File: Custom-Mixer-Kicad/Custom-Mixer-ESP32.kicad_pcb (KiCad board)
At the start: 2 copper layers, 176.3 x 110.6 mm, 21 parts, among them J1 OLED1, J2 OLED2, J3 OLED3, J4 OLED4, J5 OLED5, SW1 RotaryEncoder_Switch, SW2 RotaryEncoder_Switch, U1 ESP32-DevKitC, U2 2717

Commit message: Cad Revision
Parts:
- added G***: LOGO, Custom-Mixer-Kicad:Hackclublogo(fmask), F.Cu at (214.4, 122.5)
- added REF**: MountingHole_3.2mm_M3, MountingHole:MountingHole_3.2mm_M3, F.Cu at (75.3, 44.2)
- added REF**: MountingHole_3.2mm_M3, MountingHole:MountingHole_3.2mm_M3, F.Cu at (231.6, 134.8)
- added kibuzzard-69777CED: G***, kibuzzard-69777CED, B.Cu at (149.6, 117.7)
- added kibuzzard-69777D46: G***, kibuzzard-69777D46, B.Cu at (149.2, 111.8)
- G***: footprint Custom-Mixer-ESP32:Hackclublogo -> Custom-Mixer-Kicad:Hackclublogo
- moved G*** 2.72 mm to (214.4, 122.5)
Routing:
- net Net-(U1-GPIO23): track 122.8 -> 119.4 mm
- added copper zone on B.Cu, net GND
- added copper zone on F.Cu, net GND

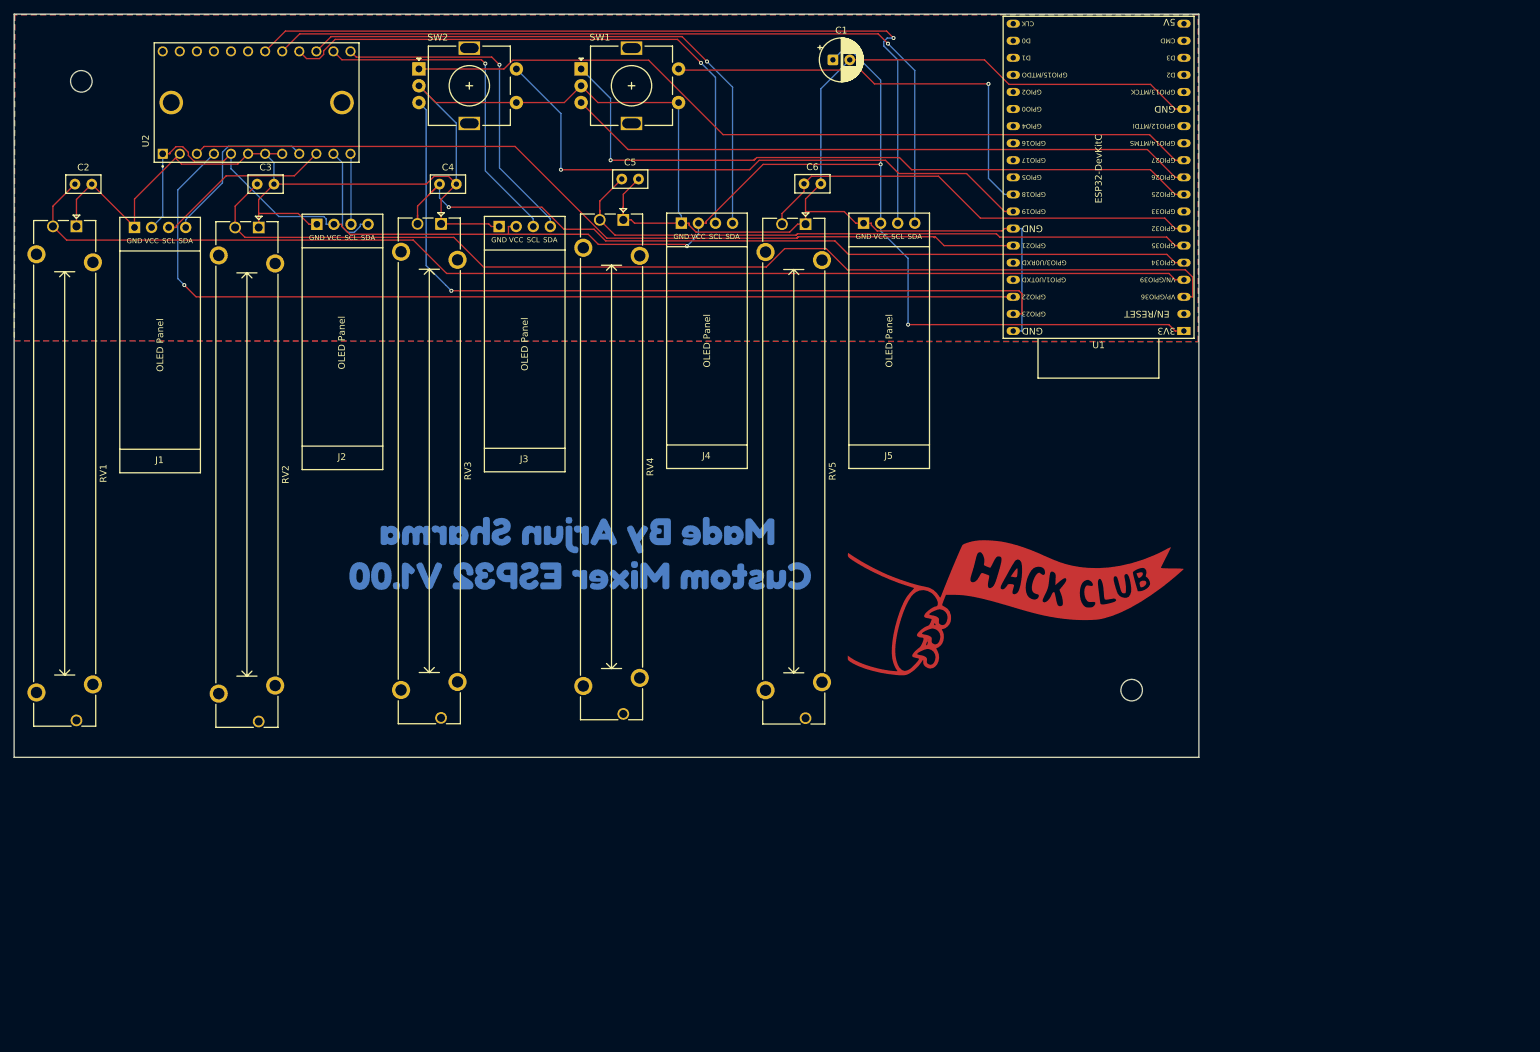
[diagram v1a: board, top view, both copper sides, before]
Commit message: Connect potentiometer pads to +3V3 and clean up nets
Updated RV2, RV3, and RV4 potentiometer pad 3 connections from unconnected nets to +3V3. Cleaned up and renumbered net assignments throughout the schematic, removed unused/unconnected net definitions, and adjusted component positions and silkscreen text for improved clarity.
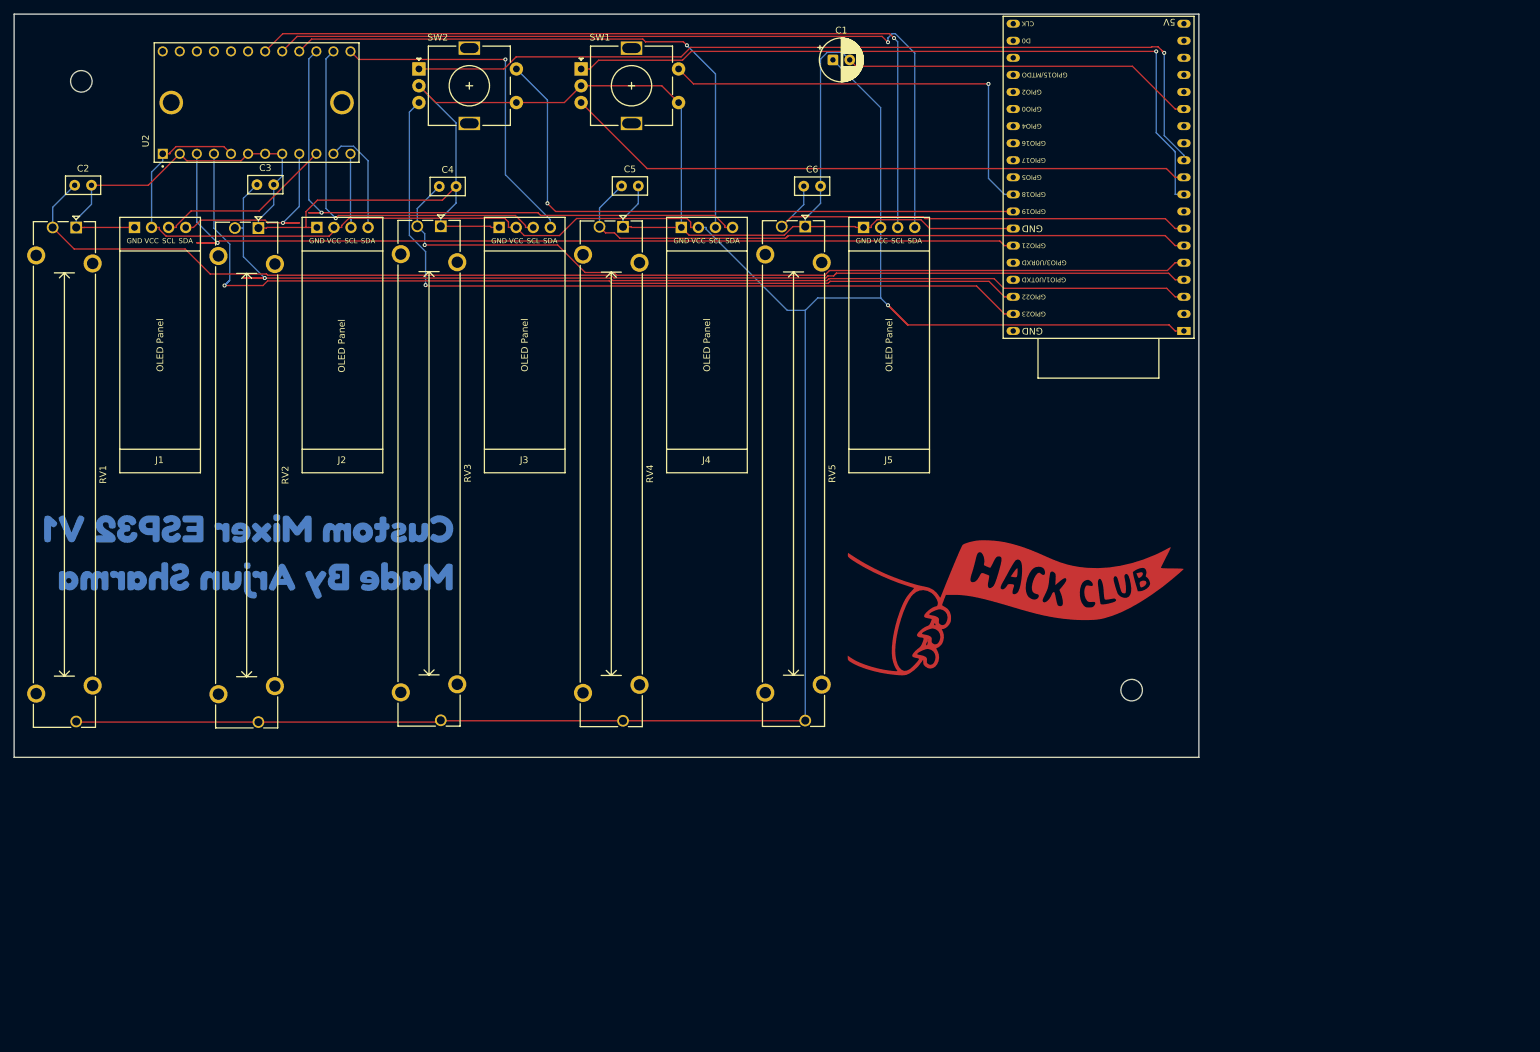
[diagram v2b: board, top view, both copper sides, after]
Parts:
- removed kibuzzard-69777CED: G***, kibuzzard-69777CED
- removed kibuzzard-69777D46: G***, kibuzzard-69777D46
- added kibuzzard-697B9E82: G***, kibuzzard-697B9E82, B.Cu at (100.2, 114.9)
- moved RV4 1.03 mm to (155.9, 65.9)
- moved C5 1.03 mm to (155.7, 59.8)
- moved J4 0.63 mm to (162.4, 102.5)
- moved J5 0.63 mm to (189.5, 102.5)
- moved J2 0.47 mm to (108.2, 102.5)
- moved C6 0.36 mm to (182.8, 59.8)
- moved RV5 0.36 mm to (183.1, 65.8)
- moved C4 0.35 mm to (128.6, 59.9)
- moved RV3 0.35 mm to (128.8, 65.8)
- moved RV1 0.17 mm to (74.6, 66.0)
- moved C2 0.17 mm to (74.4, 59.7)
- moved J3 0.14 mm to (135.3, 102.5)
- moved C3 0.09 mm to (101.5, 59.6)
- moved RV2 0.09 mm to (101.7, 66.1)
- renumbered G*** to Hackclublogo, REF** to REF1, REF** to REF2
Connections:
- RV1 pad 3: unconnected-(RV1-Pad3) -> +3V3
- RV2 pad 3: unconnected-(RV2-Pad3) -> +3V3
- RV3 pad 3: unconnected-(RV3-Pad3) -> +3V3
- RV4 pad 3: unconnected-(RV4-Pad3) -> +3V3
- RV5 pad 3: unconnected-(RV5-Pad3) -> +3V3
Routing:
- net +3V3: track 225.5 -> 415.2 mm, vias 3 -> 1
- net GND: track 357.3 -> 339.2 mm
- net Net-(U1-GPIO21): track 128.7 -> 145.6 mm, vias 0 -> 1
- net Net-(U1-ADC2_CH7/GPIO27): track 120.5 -> 131.9 mm, vias 0 -> 1
- net Net-(J1-Pin_4): track 25.7 -> 36.1 mm, vias 0 -> 1
- net Net-(J4-Pin_4): track 86.2 -> 95.1 mm
- net Net-(U1-SENSOR_VP/GPIO36/ADC1_CH0): track 159.8 -> 168.3 mm, vias 0 -> 1
- net Net-(U1-DAC_1/ADC2_CH8/GPIO25): track 103.4 -> 110.6 mm
- net Net-(J3-Pin_3): track 50.5 -> 56.3 mm
- net Net-(U1-GPIO22): track 146.2 -> 141.8 mm
- net Net-(J5-Pin_4): track 120.2 -> 123.4 mm
- net Net-(U1-GPIO19): track 88.8 -> 91.7 mm
- net Net-(U1-VDET_1/GPIO34/ADC1_CH6): track 127.7 -> 126.1 mm
- net Net-(J5-Pin_3): track 124.7 -> 123.3 mm
- net Net-(U1-VDET_2/GPIO35/ADC1_CH7): track 97.5 -> 96.1 mm
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- removed copper zone on B.Cu, net GND
- removed copper zone on F.Cu, net GND

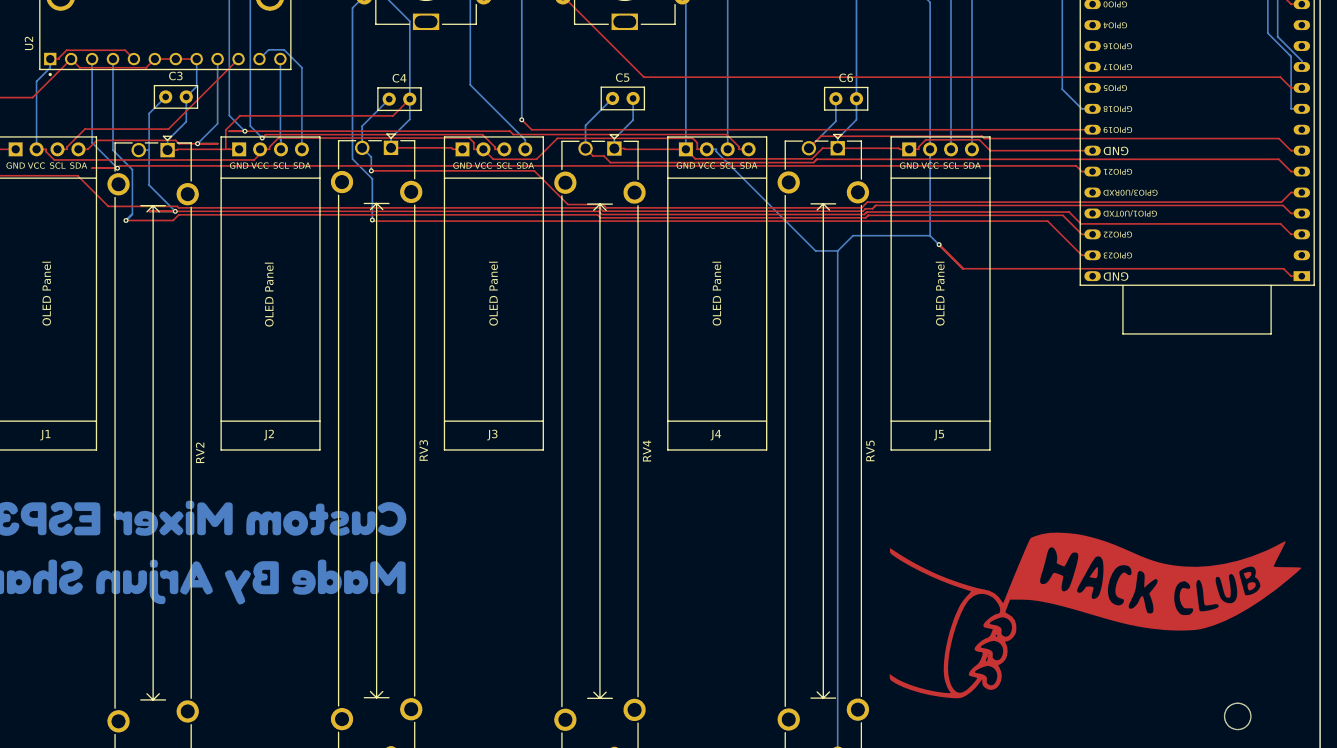
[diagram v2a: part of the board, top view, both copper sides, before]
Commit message: Add +3V3 power symbols and update PCB routing
Added multiple +3V3 power symbols to the schematic for improved clarity and power distribution. Updated PCB routing for nets 1 and 7, including new segments, vias, and changes to net connections for better signal integrity and layout. Adjusted positions of Hackclublogo footprints.
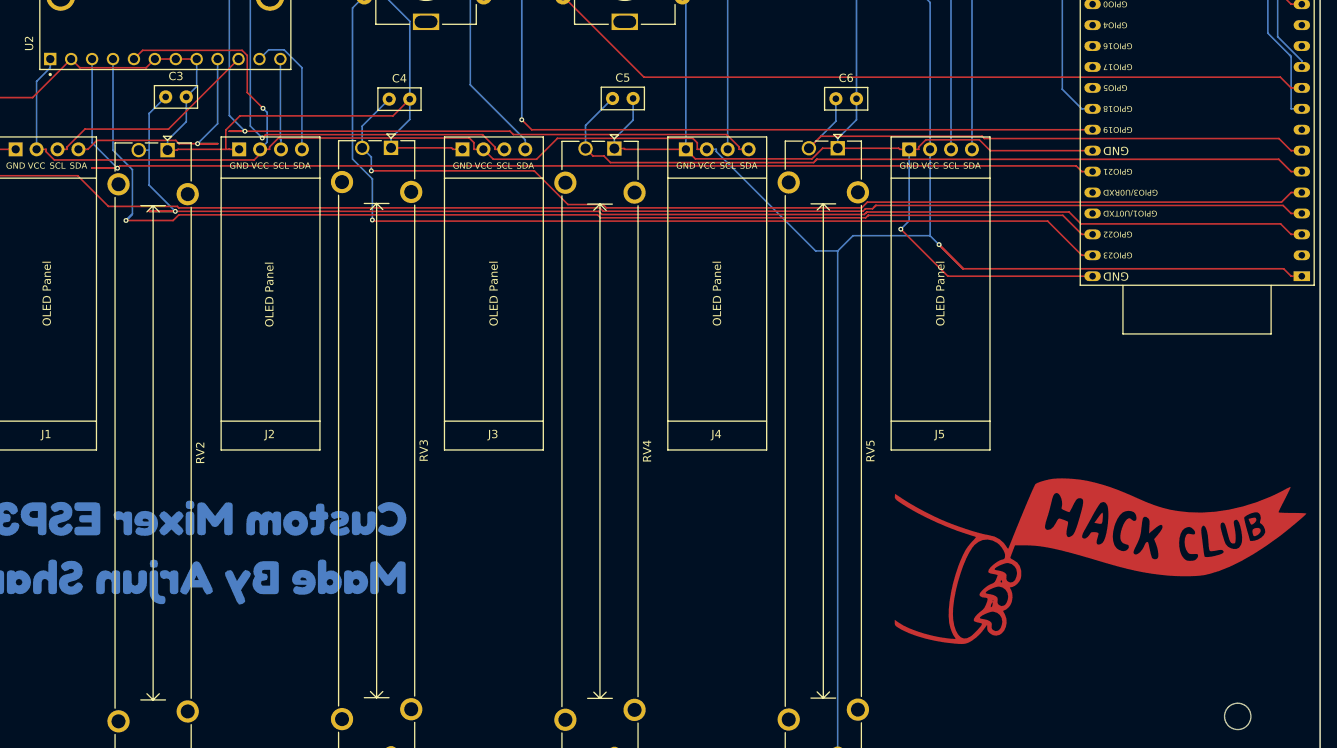
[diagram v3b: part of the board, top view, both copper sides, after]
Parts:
- moved G*** 6.62 mm to (215.0, 115.9)
- moved Hackclublogo 6.62 mm to (215.0, 115.9)
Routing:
- net GND: track 339.2 -> 374.9 mm, vias 0 -> 1
- net +3V3: track 415.2 -> 431.3 mm, vias 1 -> 2
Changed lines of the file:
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@@
 	(footprint "Custom-Mixer-Kicad:Hackclublogo(fmask)"
 		(layer "F.Cu")
-		(at 214.412172 122.459386)
+		(at 215.008372 115.87072)
 		(property "Reference" "G***"
 			(at 0 0 0)
@@
 	(footprint "Custom-Mixer-Kicad:Hackclublogo"
 		(layer "F.Cu")
-		(at 214.412172 122.459386)
+		(at 215.008372 115.87072)
 		(property "Reference" "Hackclublogo"
 			(at 0 0 0)
@@
 	)
 	(segment
+		(start 213.99 81.3634)
+		(end 196.4234 81.3634)
+		(width 0.2)
+		(layer "F.Cu")
+		(net 1)
+	)
+	(segment
 		(start 137.4978 65.96)
 		(end 136.3461 65.96)
@@
 	)
 	(segment
-		(start 201.565 66.1234)
-		(end 213.99 66.1234)
-		(width 0.2)
-		(layer "F.Cu")
-		(net 1)
-	)
-	(segment
 		(start 74.5759 65.9675)
 		(end 75.7526 65.9675)
@@
 	)
 	(segment
+		(start 201.565 66.1234)
+		(end 213.99 66.1234)
+		(width 0.2)
+		(layer "F.Cu")
+		(net 1)
+	)
+	(segment
 		(start 231.7247 41.9798)
 		(end 190.6147 41.9798)
@@
 	)
 	(segment
+		(start 196.4234 81.3634)
+		(end 190.71 75.65)
+		(width 0.2)
+		(layer "F.Cu")
+		(net 1)
+	)
+	(segment
 		(start 75.7601 65.96)
 		(end 75.7526 65.9675)
@@
 		(net 1)
 	)
+	(via
+		(at 190.71 75.65)
+		(size 0.6)
+		(drill 0.3)
+		(layers "F.Cu" "B.Cu")
+		(net 1)
+	)
 	(segment
 		(start 186.3251 39.9054)
@@
 	)
 	(segment
+		(start 190.71 75.65)
+		(end 191.7249 74.6351)
+		(width 0.2)
+		(layer "B.Cu")
+		(net 1)
+	)
+	(segment
 		(start 188.5403 39.9054)
 		(end 186.3251 39.9054)
@@
 	)
 	(segment
+		(start 191.7249 74.6351)
+		(end 191.7249 65.96)
+		(width 0.2)
+		(layer "B.Cu")
+		(net 1)
+	)
+	(segment
 		(start 105.23 58.3319)
 		(end 103.9644 59.5975)
@@
 	)
 	(segment
+		(start 111.365 54.563004)
+		(end 111.365 59.065)
+		(width 0.2)
+		(layer "F.Cu")
+		(net 7)
+	)
+	(segment
 		(start 101.6894 139.5525)
 		(end 128.6329 139.5525)
@@
 	)
 	(segment
+		(start 110.746996 53.945)
+		(end 111.365 54.563004)
+		(width 0.2)
+		(layer "F.Cu")
+		(net 7)
+	)
+	(segment
 		(start 167.1513 65.96)
 		(end 165.9996 65.96)
@@
 	)
 	(segment
-		(start 88.5057 54.868)
-		(end 89.4416 53.9321)
+		(start 98.665 53.945)
+		(end 110.746996 53.945)
 		(width 0.2)
 		(layer "F.Cu")
@@
 	)
 	(segment
+		(start 111.365 59.065)
+		(end 113.28 60.98)
+		(width 0.2)
+		(layer "F.Cu")
+		(net 7)
+	)
+	(segment
 		(start 198.2819 80.4617)
 		(end 237.1866 80.4617)
@@
 	)
 	(segment
-		(start 88.5057 55)
-		(end 88.5057 54.868)
-		(width 0.2)
-		(layer "F.Cu")
-		(net 7)
-	)
-	(segment
 		(start 112.2097 67.2505)
 		(end 113.5002 65.96)
@@
 	)
 	(segment
-		(start 87.45 55)
-		(end 88.5057 55)
+		(start 97.61 55)
+		(end 98.665 53.945)
 		(width 0.2)
 		(layer "F.Cu")
@@
 	)
 	(segment
-		(start 96.5421 53.9321)
-		(end 97.61 55)
-		(width 0.2)
-		(layer "F.Cu")
-		(net 7)
-	)
-	(segment
 		(start 138.3252 64.5846)
 		(end 138.8861 65.1455)
@@
 	)
 	(segment
-		(start 89.4416 53.9321)
-		(end 96.5421 53.9321)
-		(width 0.2)
-		(layer "F.Cu")
-		(net 7)
-	)
-	(segment
 		(start 114.076 65.96)
 		(end 114.076 65.6686)
@@
 	)
 	(via
+		(at 113.28 60.98)
+		(size 0.6)
+		(drill 0.3)
+		(layers "F.Cu" "B.Cu")
+		(net 7)
+	)
+	(via
 		(at 195.3529 77.5327)
 		(size 0.6)
@@
 	)
 	(segment
+		(start 113.788 65.0963)
+		(end 112.9243 65.96)
+		(width 0.2)
+		(layer "B.Cu")
+		(net 7)
+	)
+	(segment
 		(start 194.2649 67.0108)
 		(end 194.2649 67.1117)
@@
 	)
 	(segment
+		(start 113.28 60.98)
+		(end 113.788 61.488)
+		(width 0.2)
+		(layer "B.Cu")
+		(net 7)
+	)
+	(segment
 		(start 195.3529 77.5327)
 		(end 198.2819 80.4617)
@@
 		(width 0.2)
 		(layer "B.Cu")
+		(net 7)
+	)
+	(segment
+		(start 113.788 61.488)
+		(end 113.788 65.0963)
+		(width 0.2)
+		(layer "B.Cu")

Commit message: Update Custom-Mixer-ESP32.kicad_pcb
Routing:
- added copper zone on B.Cu, net GND
- added copper zone on F.Cu, net GND
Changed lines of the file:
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@@
 				(font
 					(size 0.001 0.001)
+					(thickness 0.15)
 				)
 				(justify mirror)
@@
 				(font
 					(size 0.001 0.001)
+					(thickness 0.15)
 				)
 				(justify mirror)
@@
 		(net 46)
 	)
+	(zone
+		(net 1)
+		(net_name "GND")
+		(layers "F.Cu" "B.Cu")
+		(hatch edge 0.5)
+		(connect_pads
+			(clearance 0.5)
+		)
+		(min_thickness 0.25)
+		(filled_areas_thickness no)
+		(fill yes
+			(thermal_gap 0.5)
+			(thermal_bridge_width 0.5)
+		)
+		(polygon
+			(pts
+				(xy 241.28 34.3) (xy 241.15 83.92) (xy 65.54 83.575) (xy 65.45 34.3)
+			)
+		)
+	)
 	(group ""
